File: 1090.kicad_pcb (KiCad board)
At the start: 2 copper layers, 235.1 x 177.8 mm, 102 parts, among them J1 Barrel_Jack, J2 J2, J3 J3, J4 J4, J5 J5, J6 J6, P1 PARALLEL_BUS_INTERFACE, U1 LM78M12, U2 LM78M05, U3 LM79M12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

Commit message: update pc board file
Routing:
- net /ID2: track 58.8 -> 51.5 mm
- net /ID1: track 64.8 -> 61.0 mm
- net /ID0: track 74.3 -> 70.5 mm
- net /D7: track 102.8 -> 99.6 mm
- net /D6: track 81.3 -> 78.4 mm
- net /B_D2: track 159.6 -> 160.7 mm
- net /B_A8: track 260.4 -> 259.5 mm
- net /D5: track 73.3 -> 72.4 mm
- net /D4: track 66.1 -> 65.4 mm
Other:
- board text added: "+10v"
- board text added: "+12v"
- board text added: "+5v"
- board text added: "-12v"
- board text added: "178mm x 227mm"
- board text added: "GND"

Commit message: change power switch to c&k e101
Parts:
- S1: footprint 1090:SPDT_Horiz_Rocker_Switch -> footprints:E101J1ABE2
- moved S1 18.4 mm to (519.8, 175.3)
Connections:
- S1 pad 4: (no net) -> GND
- S1 pad 5: (no net) -> GND
- S1 pad 6: (no net) -> GND
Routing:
- net GND: track 4086.6 -> 4092.4 mm
- net /PR1: track 29.0 -> 33.8 mm
- net /PR3: track 34.1 -> 34.8 mm

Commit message: numerous changes to schematic and board files
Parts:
- moved S1 0.92 mm to (519.7, 176.2)
- moved REF** 0.31 mm to (367.2, 160.3)
- moved REF** 0.27 mm to (474.6, 160.3)
- moved REF** 0.21 mm to (338.9, 160.3)
- moved REF** 0.19 mm to (314.0, 160.3)
- moved REF** 0.17 mm to (342.3, 160.3)
- moved REF** 0.12 mm to (449.6, 160.3)
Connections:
- REF** pad : GND -> (no net)
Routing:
- net /PR3: track 34.8 -> 35.9 mm
- net /Pin47: track 284.8 -> 285.7 mm
- net GND: track 4092.4 -> 4091.7 mm
- net /PR1: track 33.8 -> 34.3 mm

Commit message: various board fixes
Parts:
- moved C11 0.08 mm to (350.9, 143.5)
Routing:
- net +10V: track 807.7 -> 779.8 mm
- net GND: track 4091.7 -> 4089.5 mm
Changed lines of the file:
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@@
   (general
     (thickness 1.6)
-    (drawings 47)
-    (tracks 3290)
+    (drawings 48)
+    (tracks 3287)
     (zones 0)
     (modules 102)
@@
       (effects (font (size 0.127 0.127) (thickness 0.002)))
     )
-    (pad 4 thru_hole circle (at 12.7 -2.54 90) (size 2.8956 2.8956) (drill 2.3876) (layers *.Cu *.Mask)
+    (pad 5 thru_hole circle (at 12.7 7.62 90) (size 3.2 3.2) (drill 2.3876) (layers *.Cu *.Mask)
       (net 3 GND))
-    (pad 7 thru_hole circle (at 12.7 12.7 90) (size 2.8956 2.8956) (drill 2.3876) (layers *.Cu *.Mask)
+    (pad 4 thru_hole circle (at 12.7 2.54 90) (size 3.2 3.2) (drill 2.3876) (layers *.Cu *.Mask)
       (net 3 GND))
-    (pad 6 thru_hole circle (at 12.7 7.62 90) (size 2.8956 2.8956) (drill 2.3876) (layers *.Cu *.Mask)
-      (net 3 GND))
-    (pad 5 thru_hole circle (at 12.7 2.54 90) (size 2.8956 2.8956) (drill 2.3876) (layers *.Cu *.Mask)
-      (net 3 GND))
-    (pad 3 thru_hole circle (at 0 9.400001) (size 1.524 1.524) (drill 1.016) (layers *.Cu *.Mask))
-    (pad 2 thru_hole circle (at 0 4.700001) (size 1.524 1.524) (drill 1.016) (layers *.Cu *.Mask)
+    (pad 3 thru_hole circle (at 0 9.400001) (size 2.524 2.524) (drill 1.85) (layers *.Cu *.Mask))
+    (pad 2 thru_hole circle (at 0 4.700001) (size 2.524 2.524) (drill 1.85) (layers *.Cu *.Mask)
       (net 112 /PR3))
-    (pad 1 thru_hole circle (at 0 0) (size 1.524 1.524) (drill 1.016) (layers *.Cu *.Mask)
+    (pad 1 thru_hole circle (at 0 0) (size 2.524 2.524) (drill 1.85) (layers *.Cu *.Mask)
       (net 118 /PR1))
   )
@@
     (descr "C, Axial series, Axial, Horizontal, pin pitch=12.5mm, , length*diameter=5.1*3.1mm^2, http://www.vishay.com/docs/45231/arseries.pdf")
     (tags "C Axial series Axial Horizontal pin pitch 12.5mm  length 5.1mm diameter 3.1mm")
-    (fp_text reference C23 (at 0 2.286 180) (layer F.SilkS)
+    (fp_text reference C23 (at 15.23 -0.04 180) (layer F.SilkS)
       (effects (font (size 1 1) (thickness 0.15)))
     )
@@
   )
   (module Capacitor_THT:CP_Radial_D12.5mm_P5.00mm (layer F.Cu)
-    (at 350.805 143.545 90)
+    (at 350.88 143.54 90)
     (descr "CP, Radial series, Radial, pin pitch=5.00mm, , diameter=12.5mm, Electrolytic Capacitor")
     (tags "CP Radial series Radial pin pitch 5.00mm  diameter 12.5mm Electrolytic Capacitor")
@@
     (descr "C, Axial series, Axial, Horizontal, pin pitch=12.5mm, , length*diameter=5.1*3.1mm^2, http://www.vishay.com/docs/45231/arseries.pdf")
     (tags "C Axial series Axial Horizontal pin pitch 12.5mm  length 5.1mm diameter 3.1mm")
-    (fp_text reference CR13 (at 15.755 0.046) (layer F.SilkS)
+    (fp_text reference CR13 (at 14.843 -1.168) (layer F.SilkS)
       (effects (font (size 1 1) (thickness 0.15)))
     )
@@
     (descr "solder Pin_ diameter 1.0mm, hole diameter 1.0mm (press fit), length 10.0mm")
     (tags "solder Pin_ press fit")
-    (fp_text reference TP3 (at 3.048 0.762) (layer F.SilkS)
+    (fp_text reference TP3 (at 3.035 -1.79) (layer F.SilkS)
       (effects (font (size 1 1) (thickness 0.15)))
     )
@@
     )
   )
+  (gr_text GND (at 343.43 132.79) (layer F.SilkS)
+    (effects (font (size 1 1) (thickness 0.15)))
+  )
   (gr_text GND (at 504.52274 180.36032) (layer F.SilkS)
     (effects (font (size 1 1) (thickness 0.15)))
@@
     (effects (font (size 1 1) (thickness 0.15)))
   )
-  (gr_text +5v (at 334.07604 181.86146) (layer F.SilkS)
-    (effects (font (size 1 1) (thickness 0.15)))
+  (gr_text +5v (at 334.69 182.49) (layer F.SilkS)
+    (effects (font (size 1.5 1.5) (thickness 0.2)))
   )
   (gr_text "178mm x 227mm" (at 316.45606 119.2657) (layer F.SilkS)
@@
   (segment (start 343.755 140.245) (end 328.18 140.245) (width 1.016) (layer B.Cu) (net 2))
   (segment (start 345.455 138.545) (end 343.755 140.245) (width 1.016) (layer B.Cu) (net 2))
-  (segment (start 328.255 140.995) (end 328.18 141.07) (width 1.016) (layer B.Cu) (net 2))
-  (segment (start 470.577 133.63) (end 469.47 133.63) (width 1.016) (layer B.Cu) (net 2))
-  (segment (start 471.44 132.767) (end 470.577 133.63) (width 1.016) (layer B.Cu) (net 2))
-  (segment (start 469.47 133.63) (end 464.58 138.52) (width 1.016) (layer B.Cu) (net 2))
-  (segment (start 464.58 138.52) (end 335.905 138.52) (width 1.016) (layer B.Cu) (net 2))
-  (segment (start 345.855 139.52) (end 344.38 140.995) (width 1.016) (layer B.Cu) (net 2))
-  (segment (start 344.38 140.995) (end 328.255 140.995) (width 1.016) (layer B.Cu) (net 2))
   (segment (start 489.305 139.77) (end 481.18 139.77) (width 1.016) (layer B.Cu) (net 2))
   (segment (start 489.455 139.62) (end 489.305 139.77) (width 1.016) (layer B.Cu) (net 2))
@@
   (segment (start 511.26 189.2) (end 499.61 189.2) (width 1.016) (layer B.Cu) (net 2))
   (segment (start 512.17 190.11) (end 511.26 189.2) (width 1.016) (layer B.Cu) (net 2))
-  (segment (start 532.511 172.72) (end 532.511 173.59999) (width 0.25) (layer B.Cu) (net 3))
+  (segment (start 345.49 138.52) (end 345.48 138.53) (width 1.016) (layer B.Cu) (net 2))
+  (segment (start 464.58 138.52) (end 345.49 138.52) (width 1.016) (layer B.Cu) (net 2))
+  (segment (start 469.47 133.63) (end 464.58 138.52) (width 1.016) (layer B.Cu) (net 2))
+  (segment (start 470.577 133.63) (end 469.47 133.63) (width 1.016) (layer B.Cu) (net 2))
+  (segment (start 471.44 132.767) (end 470.577 133.63) (width 1.016) (layer B.Cu) (net 2))
   (segment (start 338.605 160.07) (end 341.955 160.07) (width 1.016) (layer F.Cu) (net 3))
   (segment (start 338.58 161.1) (end 338.58 159.24) (width 1.016) (layer F.Cu) (net 3))
@@
   (segment (start 532.39 183.7884) (end 532.39 178.7204) (width 2.8956) (layer B.Cu) (net 3))
   (segment (start 532.384 183.7944) (end 532.39 183.7884) (width 2.8956) (layer B.Cu) (net 3))
-  (segment (start 532.39 173.6404) (end 532.39 178.5552) (width 2.8956) (layer B.Cu) (net 3))
-  (segment (start 532.384 173.6344) (end 532.39 173.6404) (width 2.8956) (layer B.Cu) (net 3))
+  (segment (start 532.39 175.012) (end 532.39 178.5552) (width 2.8956) (layer B.Cu) (net 3))
+  (segment (start 532.384 175.006) (end 532.39 175.012) (width 2.8956) (layer B.Cu) (net 3))
   (segment (start 419.32837 184.818) (end 419.34937 184.797) (width 1.016) (layer B.Cu) (net 4))
   (segment (start 418.197 184.818) (end 419.32837 184.818) (width 1.016) (layer B.Cu) (net 4))

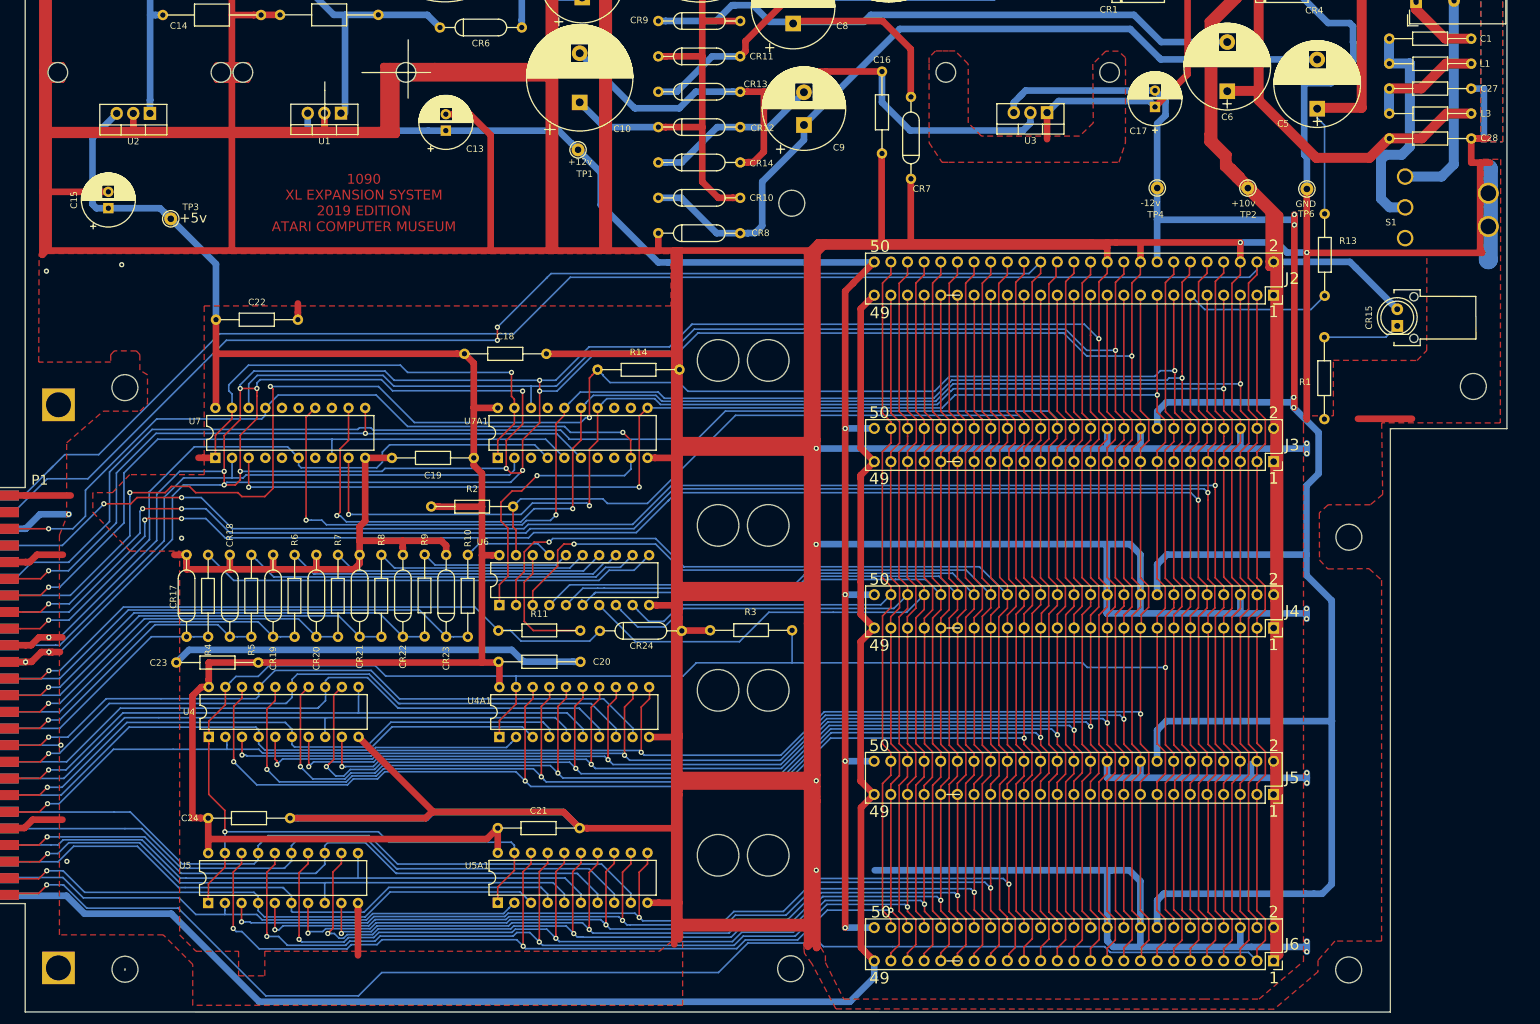
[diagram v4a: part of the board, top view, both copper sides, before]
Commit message: included many changes by pancio, update schematic and pcb to fix all DRC errors
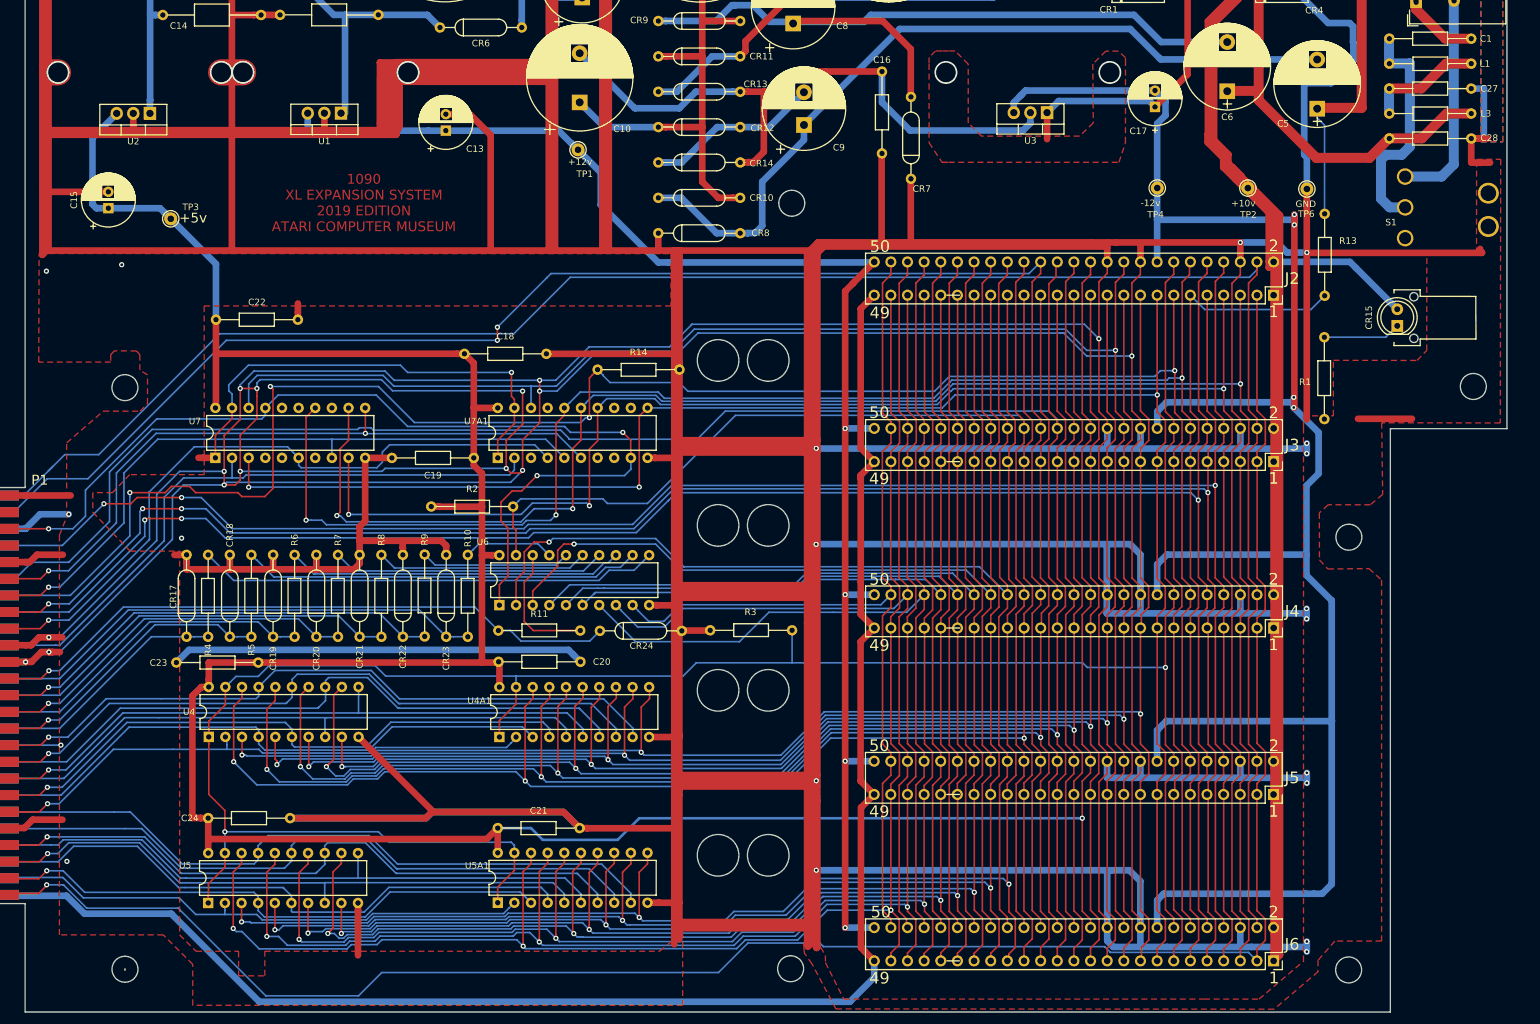
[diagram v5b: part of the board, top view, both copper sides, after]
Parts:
- removed ? (x2): , 1090:test
- removed REF** (x6): MountingHole_2.5mm, MountingHole:MountingHole_2.5mm
- C3, C4, C7: footprint Capacitor_THT:CP_Radial_D22.0mm_P10.00mm_SnapIn -> 1090:CP_Radial_D22.0mm_P10.00mm_SnapIn
- C5, C6: footprint Capacitor_THT:CP_Radial_D13.0mm_P7.50mm -> 1090:CP_Radial_D13.0mm_P7.50mm
- CR1: footprint Diode_THT:D_5KP_P10.16mm_Horizontal -> 1090:D_5KP_P10.16mm_Horizontal
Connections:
- J2 pad 24: /+5V_REF -> +5V
- J2 pad 26: (no net) -> /rsvd
- J3 pad 24: /+5V_REF -> +5V
- J3 pad 26: (no net) -> /rsvd
- J4 pad 24: /+5V_REF -> +5V
- J4 pad 26: (no net) -> /rsvd
- J5 pad 24: /+5V_REF -> +5V
- J5 pad 26: (no net) -> /rsvd
- J6 pad 24: /+5V_REF -> +5V
- J6 pad 26: (no net) -> /rsvd
- S1 pad 4: GND -> (no net)
- S1 pad 5: GND -> (no net)
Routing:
- net +5V: track 290.2 -> 487.3 mm, vias 0 -> 1
- net /+5V_REF: track 105.8 -> 0.00 mm
- net /rsvd: track 0.00 -> 105.8 mm
- net (no net): track 105.8 -> 0.00 mm, vias 4 -> 6
- net GND: track 4089.5 -> 4047.4 mm, vias 33 -> 37

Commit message: fixed width of 50 pin edgecard connector
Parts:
- moved P1 0.94 mm to (305.6, 244.2)
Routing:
- net /A3: track 100.2 -> 95.5 mm
- net /!EXTSEL: track 306.9 -> 310.4 mm
- net /Pin47: track 285.7 -> 282.5 mm
- net GND: track 4047.4 -> 4046.2 mm
- net /A10: track 96.1 -> 95.3 mm
- net /A8: track 87.0 -> 86.3 mm
- net /A14: track 107.1 -> 106.4 mm
- net /A2: track 94.8 -> 94.2 mm
- net /A11: track 96.4 -> 95.8 mm
- net /A13: track 104.3 -> 103.8 mm
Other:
- outline, holes or cut-outs redrawn
